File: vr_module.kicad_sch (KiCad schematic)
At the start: 44 parts

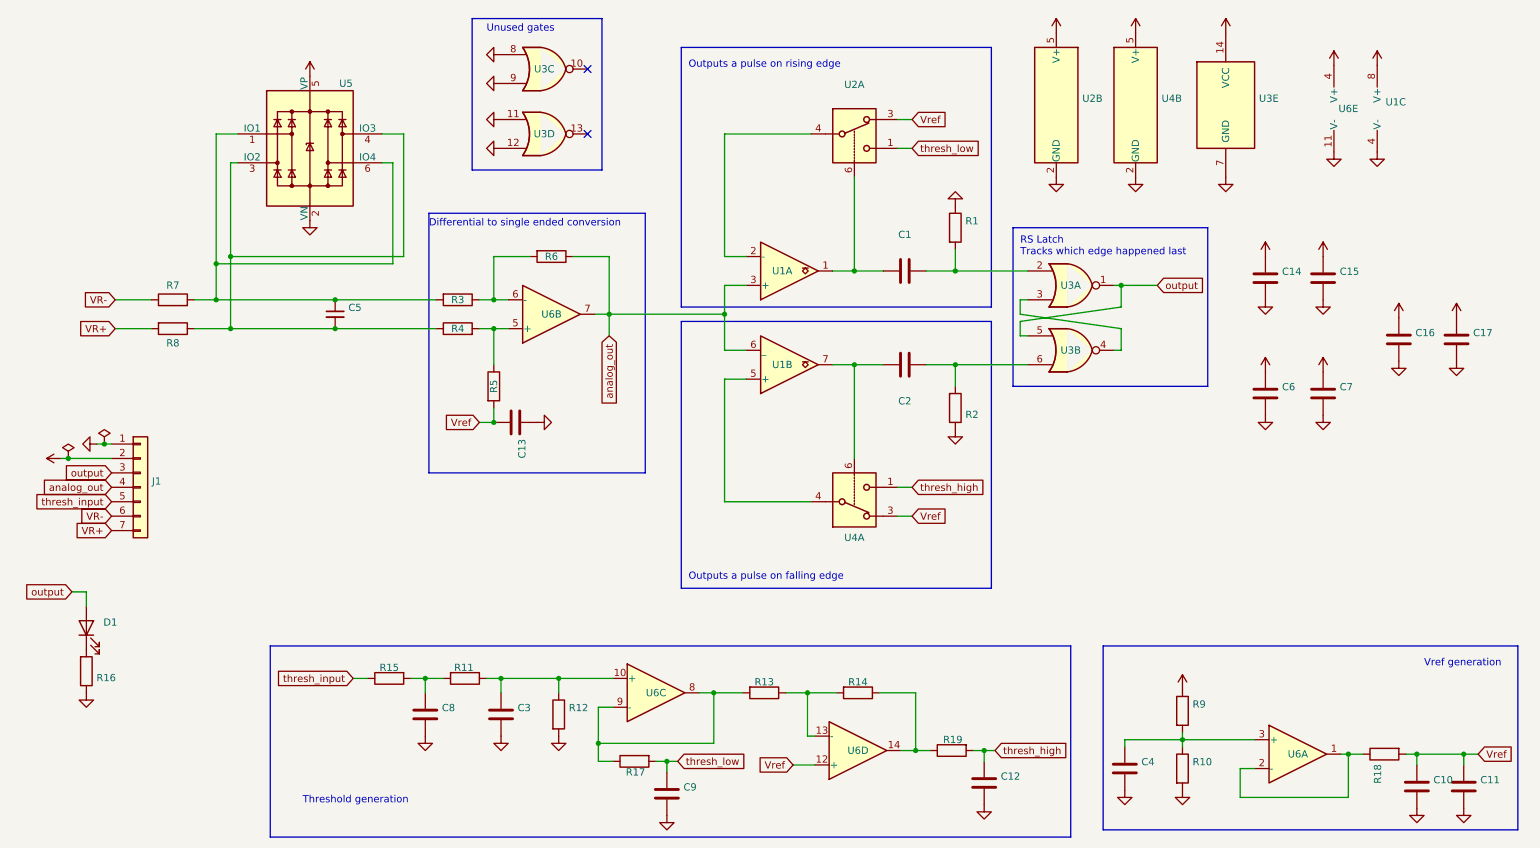
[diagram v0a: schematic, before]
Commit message: Draft single ended supply option.
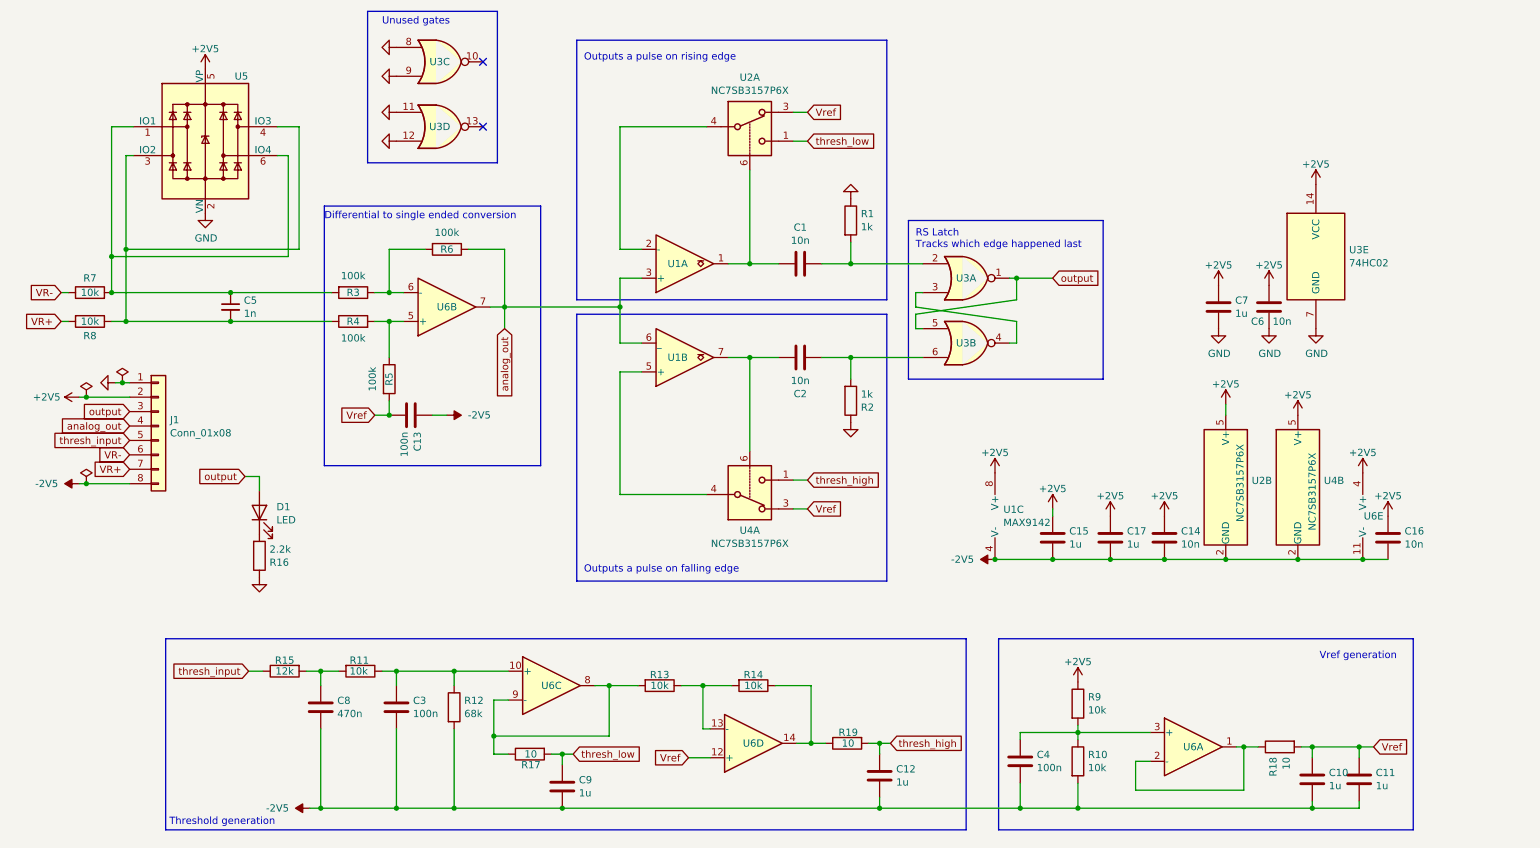
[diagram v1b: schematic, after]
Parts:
- C1, C14, C16, C2, C6: value (none) -> 10n; footprint (none) -> Capacitor_SMD:C_0402_1005Metric
- C10, C11, C12, C15, C17, C7, C9: value (none) -> 1u; footprint (none) -> Capacitor_SMD:C_0402_1005Metric
- C13, C3, C4: value (none) -> 100n; footprint (none) -> Capacitor_SMD:C_0402_1005Metric
- C5: value (none) -> 1n; footprint (none) -> Capacitor_SMD:C_0402_1005Metric
- C8: value (none) -> 470n; footprint (none) -> Capacitor_SMD:C_0402_1005Metric
- D1: value (none) -> LED; footprint (none) -> LED_SMD:LED_0603_1608Metric
- J1: value (none) -> Conn_01x08; footprint (none) -> Connector_PinHeader_2.54mm:PinHeader_1x07_P2.54mm_Vertical; symbol Connector_Generic:Conn_01x07 -> Connector_Generic:Conn_01x08
- R1, R2: value (none) -> 1k; footprint (none) -> Resistor_SMD:R_0402_1005Metric
- R10, R11, R13, R14, R9: value (none) -> 10k; footprint (none) -> Resistor_SMD:R_0402_1005Metric
- R12: value (none) -> 68k; footprint (none) -> Resistor_SMD:R_0402_1005Metric
- R15: value (none) -> 12k; footprint (none) -> Resistor_SMD:R_0402_1005Metric
- R16: value (none) -> 2.2k; footprint (none) -> Resistor_SMD:R_0402_1005Metric
- R17, R18, R19: value (none) -> 10; footprint (none) -> Resistor_SMD:R_0402_1005Metric
- R3, R4, R5, R6: value (none) -> 100k; footprint (none) -> Resistor_SMD:R_0402_1005Metric
- R7, R8: value (none) -> 10k; footprint (none) -> Resistor_SMD:R_0805_2012Metric
- U1: value (none) -> MAX9142; footprint (none) -> Package_SO:SOIC-8_3.9x4.9mm_P1.27mm
- U2, U4: value (none) -> NC7SB3157P6X; footprint (none) -> Package_TO_SOT_SMD:SOT-363_SC-70-6
- U3: value (none) -> 74HC02; footprint (none) -> Package_SO:SOIC-14_3.9x8.7mm_P1.27mm
- U5: value (none) -> SRV05-4; footprint (none) -> Package_TO_SOT_SMD:SOT-23-6
- U6: value (none) -> MCP6004; footprint (none) -> Package_SO:TSSOP-14_4.4x5mm_P0.65mm
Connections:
- net GND: no longer C10.2, C11.2, C12.2, C13.1, C14.2, C15.2, C16.2, C17.2, C3.2, C4.2, C8.2, C9.2, R10.2, R12.2, U1.4 (V-), U2.2 (GND), U4.2 (GND), U6.11 (V-)
- net +5V renamed +2V5
- new net -2V5: C10.2, C11.2, C12.2, C13.1, C14.2, C15.2, C16.2, C17.2, C3.2, C4.2, C8.2, C9.2, J1.8 (Pin_8), R10.2, R12.2, U1.4 (V-), U2.2 (GND), U4.2 (GND), U6.11 (V-)
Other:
- company: (none) -> rusEFI
- title: (none) -> VR for rusEFI
- moved on the sheet: C1, C10, C11, C12, C13, C14, C15, C16, C17, C2, C3, C4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
